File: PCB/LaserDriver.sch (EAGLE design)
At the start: 23 parts, among them IC1 OPA27U, IC2 7805T, Q1 IRF510

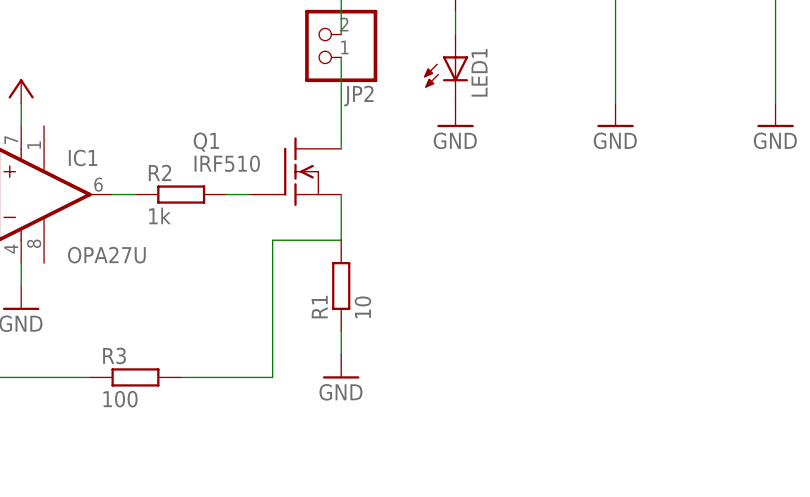
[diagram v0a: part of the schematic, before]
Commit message: Fixed component placement issues and modified directory tree.
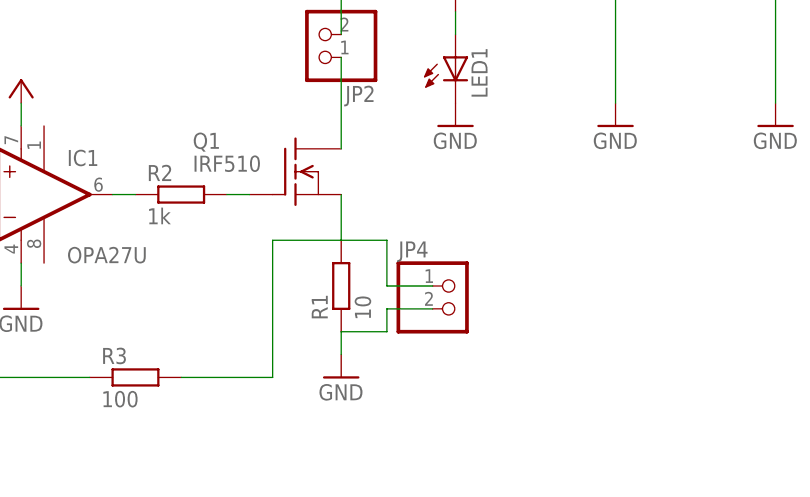
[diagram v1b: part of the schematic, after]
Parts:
- added JP4: (no value), pinhead:PINHD-1X2
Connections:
- net GND: now also JP4.2
- net N$1: now also JP4.1
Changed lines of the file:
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@@
 <part name="R9" library="rcl" deviceset="R-EU_" device="R1206" value="1k"/>
 <part name="GND12" library="supply1" deviceset="GND" device=""/>
+<part name="JP4" library="pinhead" deviceset="PINHD-1X2" device=""/>
 </parts>
 <sheets>
@@
 <instance part="R9" gate="G$1" x="96.52" y="104.14" rot="R90"/>
 <instance part="GND12" gate="1" x="96.52" y="86.36"/>
+<instance part="JP4" gate="G$1" x="96.52" y="66.04"/>
 </instances>
 <busses>
@@
 <pinref part="GND2" gate="1" pin="GND"/>
 <wire x1="83.82" y1="60.96" x2="83.82" y2="63.5" width="0.1524" layer="91"/>
+<pinref part="JP4" gate="G$1" pin="2"/>
+<wire x1="93.98" y1="66.04" x2="88.9" y2="66.04" width="0.1524" layer="91"/>
+<wire x1="88.9" y1="66.04" x2="88.9" y2="63.5" width="0.1524" layer="91"/>
+<wire x1="88.9" y1="63.5" x2="83.82" y2="63.5" width="0.1524" layer="91"/>
 </segment>
 <segment>
@@
 <pinref part="R3" gate="G$1" pin="2"/>
 <wire x1="76.2" y1="58.42" x2="66.04" y2="58.42" width="0.1524" layer="91"/>
+<wire x1="83.82" y1="73.66" x2="88.9" y2="73.66" width="0.1524" layer="91"/>
+<wire x1="88.9" y1="73.66" x2="88.9" y2="68.58" width="0.1524" layer="91"/>
+<pinref part="JP4" gate="G$1" pin="1"/>
+<wire x1="88.9" y1="68.58" x2="93.98" y2="68.58" width="0.1524" layer="91"/>
 </segment>
 </net>
